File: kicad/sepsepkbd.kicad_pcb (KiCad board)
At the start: 2 copper layers, 162.2 x 115 mm, 62 parts, among them J1 Conn_01x10_Pin, J2 MJ-4PP-9, J3 Conn_01x08_Pin, J4 Conn_01x10_Pin, J5 MJ-4PP-9, J6 Conn_01x08_Pin, J9 Conn_01x10_Pin, SW1 SW_PUSH, SW10 SW_PUSH, SW11 SW_PUSH, SW12 SW_PUSH, SW13 SW_PUSH, SW14 SW_PUSH, SW15 SW_PUSH, SW16 SW_PUSH, SW17 SW_PUSH, SW18 SW_PUSH, SW19 SW_PUSH, SW2 SW_PUSH, SW20 SW_PUSH, SW21 SW_PUSH, SW22 SW_PUSH, SW23 SW_PUSH, SW24 SW_PUSH, SW25 SW_PUSH, SW3 SW_PUSH, SW4 SW_PUSH, SW5 SW_PUSH, SW6 SW_PUSH, SW7 SW_PUSH, SW8 SW_PUSH, SW9 SW_PUSH, U1 RP2040-Zero, U2 RP2040-Zero

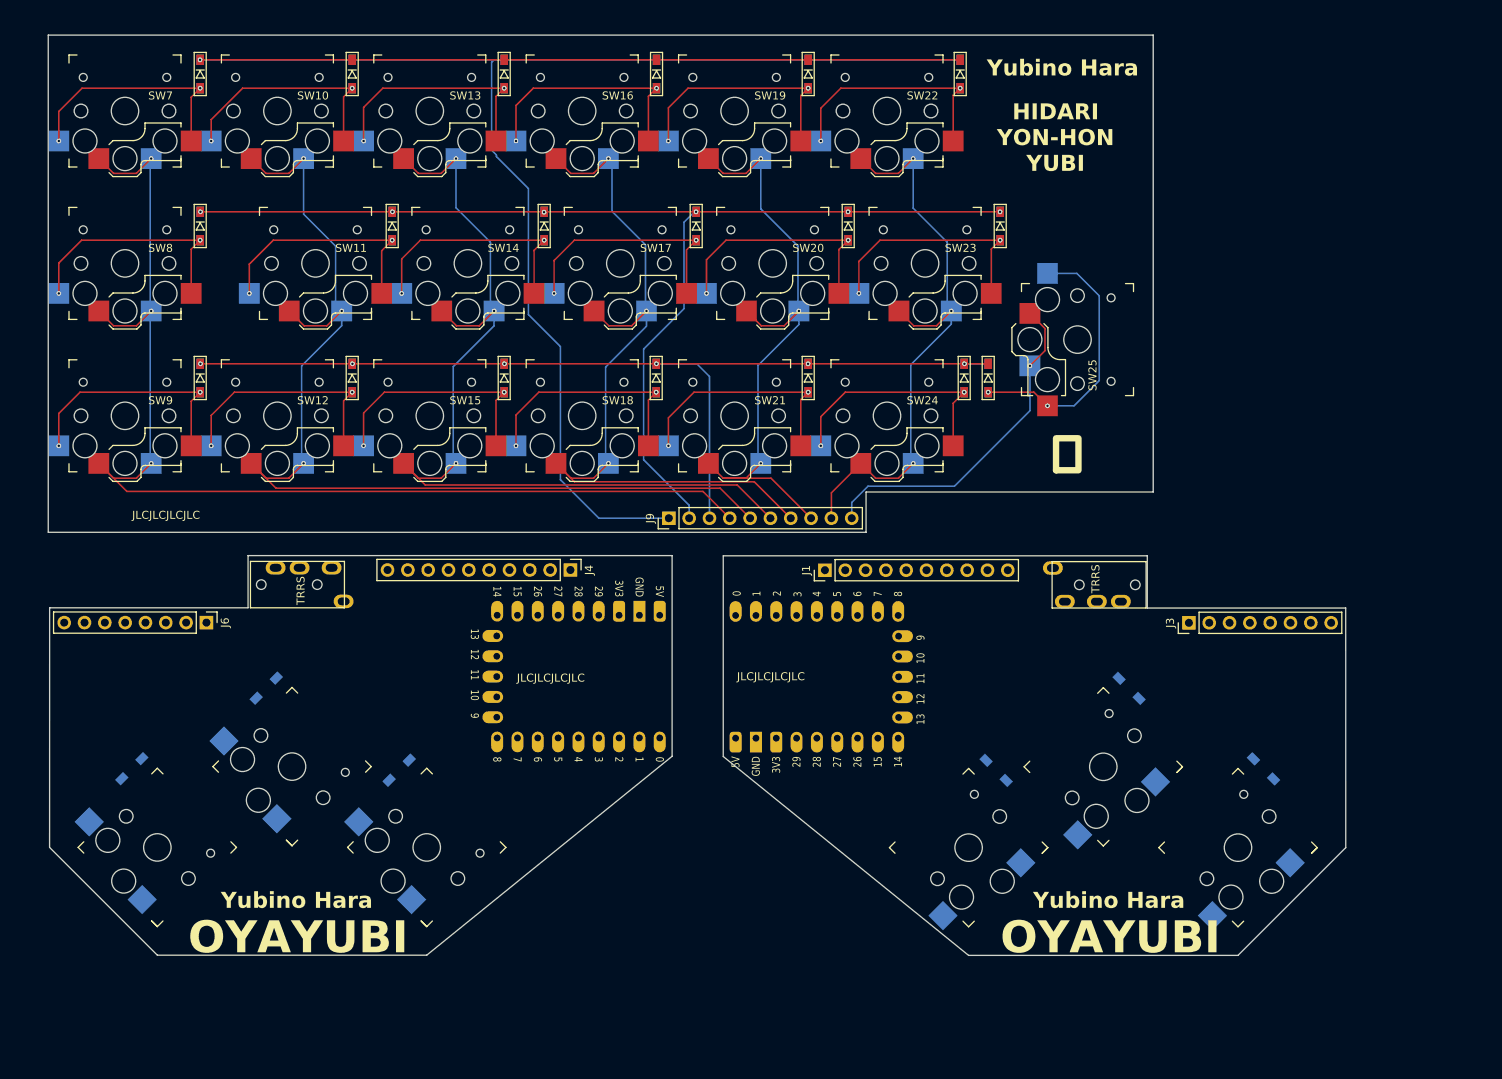
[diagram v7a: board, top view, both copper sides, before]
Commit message: Add LEDs, and convert RP2040 to SMD
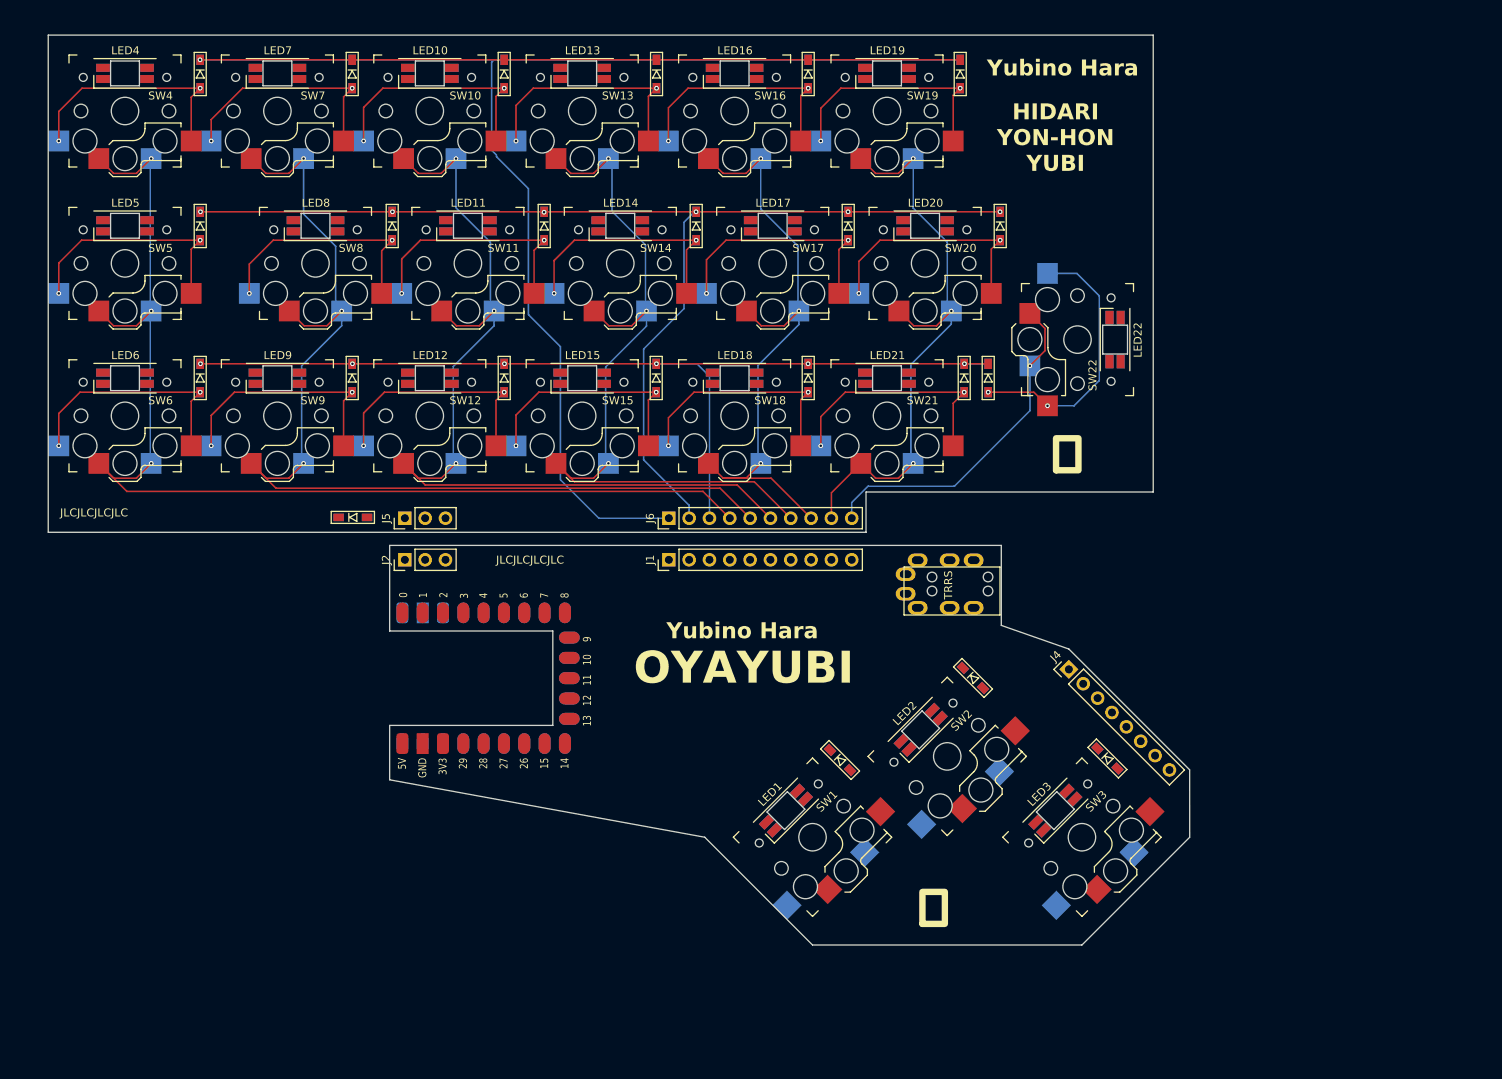
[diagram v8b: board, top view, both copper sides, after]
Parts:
- removed the D4 at (29.9, 109.3)
- removed the D5 at (63.3, 109.5)
- removed the D6 at (46.7, 99.2)
- removed the J4 at (84.7, 84.5)
- removed the J6 at (39.2, 91.0)
- removed the REF** at (48.7, 129.4)
- removed the REF** at (150.2, 129.4)
- removed the SW4 at (33.1, 119.2)
- removed the SW5 at (49.9, 109.0)
- removed the SW6 at (66.7, 119.2)
- removed U2: RP2040-Zero, isw-kbd:RP2040-Zero-THT
- added D23: D, kbd:D3_SMD, F.Cu at (57.5, 77.9)
- added J2: Conn_01x03_Pin, Connector_PinHeader_2.54mm:PinHeader_1x03_P2.54mm_Vertical, F.Cu at (64.0, 83.2)
- added LED1: YS-SK6812MINI-E, sepsepkbd:YS-SK6812MINI-E, F.Cu at (111.6, 114.6)
- added LED10: YS-SK6812MINI-E, sepsepkbd:YS-SK6812MINI-E, F.Cu at (67.1, 22.4)
- added LED11: YS-SK6812MINI-E, sepsepkbd:YS-SK6812MINI-E, F.Cu at (71.9, 41.5)
- added LED12: YS-SK6812MINI-E, sepsepkbd:YS-SK6812MINI-E, F.Cu at (67.1, 60.5)
- added LED13: YS-SK6812MINI-E, sepsepkbd:YS-SK6812MINI-E, F.Cu at (86.2, 22.4)
- added LED14: YS-SK6812MINI-E, sepsepkbd:YS-SK6812MINI-E, F.Cu at (90.9, 41.5)
- added LED15: YS-SK6812MINI-E, sepsepkbd:YS-SK6812MINI-E, F.Cu at (86.2, 60.5)
- added LED16: YS-SK6812MINI-E, sepsepkbd:YS-SK6812MINI-E, F.Cu at (105.2, 22.4)
- added LED17: YS-SK6812MINI-E, sepsepkbd:YS-SK6812MINI-E, F.Cu at (110.0, 41.5)
- added LED18: YS-SK6812MINI-E, sepsepkbd:YS-SK6812MINI-E, F.Cu at (105.2, 60.5)
- added LED19: YS-SK6812MINI-E, sepsepkbd:YS-SK6812MINI-E, F.Cu at (124.3, 22.4)
- added LED2: YS-SK6812MINI-E, sepsepkbd:YS-SK6812MINI-E, F.Cu at (128.5, 104.5)
- added LED20: YS-SK6812MINI-E, sepsepkbd:YS-SK6812MINI-E, F.Cu at (129.0, 41.5)
- added LED21: YS-SK6812MINI-E, sepsepkbd:YS-SK6812MINI-E, F.Cu at (124.3, 60.5)
- added LED22: YS-SK6812MINI-E, sepsepkbd:YS-SK6812MINI-E, F.Cu at (152.8, 55.7)
- added LED3: YS-SK6812MINI-E, sepsepkbd:YS-SK6812MINI-E, F.Cu at (145.3, 114.6)
- added LED4: YS-SK6812MINI-E, sepsepkbd:YS-SK6812MINI-E, F.Cu at (29.0, 22.4)
- added LED5: YS-SK6812MINI-E, sepsepkbd:YS-SK6812MINI-E, F.Cu at (29.0, 41.5)
- added LED6: YS-SK6812MINI-E, sepsepkbd:YS-SK6812MINI-E, F.Cu at (29.0, 60.5)
- added LED7: YS-SK6812MINI-E, sepsepkbd:YS-SK6812MINI-E, F.Cu at (48.1, 22.4)
- added LED8: YS-SK6812MINI-E, sepsepkbd:YS-SK6812MINI-E, F.Cu at (52.8, 41.5)
- added LED9: YS-SK6812MINI-E, sepsepkbd:YS-SK6812MINI-E, F.Cu at (48.1, 60.5)
- added REF**: ThumbsBoard_logo, sepsepkbd:ThumbsBoard_logo, F.Cu at (105.1, 94.3)
- added REF**: ThumbsBoard_logo, sepsepkbd:ThumbsBoard_logo, B.Cu at (105.3, 94.3)
- D1, D2, D3: footprint kbd:D3_SMD_v2 -> kbd:D3_SMD
- J3: renamed from J2; footprint kbd:MJ-4PP-9_1side -> kbd:MJ-4PP-9
- J5: value MJ-4PP-9 -> Conn_01x03_Pin; footprint kbd:MJ-4PP-9_1side -> Connector_PinHeader_2.54mm:PinHeader_1x03_P2.54mm_Vertical
- SW1, SW2, SW3: footprint keyswitches:Kailh_socket_PG1350 -> keyswitches:Kailh_socket_PG1350_reversible
- U1: footprint isw-kbd:RP2040-Zero-THT -> sepsepkbd:WS-RP2040-Zero SMD
- moved U1 41.7 mm to (73.8, 98.0)
- moved J5 21.1 mm to (64.0, 78.0)
- moved D1 19.6 mm to (151.8, 108.0)
- moved D2 19.6 mm to (135.0, 98.0)
- moved D3 19.6 mm to (118.4, 108.2)
- moved J1 19.6 mm to (97.0, 83.2)
- moved SW1 19.6 mm to (115.0, 117.9)
- moved SW2 19.6 mm to (131.8, 107.8)
- moved SW3 19.6 mm to (148.6, 117.9)
- moved J3 18.4 mm to (138.4, 87.1)
- moved J4 16.1 mm to (147.0, 96.9), turned to 45 degrees
- renumbered D13 to D10, D14 to D11, D15 to D12, D16 to D13, D17 to D14, D18 to D15, D19 to D16, D20 to D17, D21 to D18, D22 to D19, D23 to D20, D24 to D21, D25 to D22, D7 to D4, D8 to D5, D9 to D6, D10 to D7, D11 to D8, D12 to D9, J3 to J4, J9 to J6, SW13 to SW10, SW14 to SW11, SW15 to SW12, SW16 to SW13, SW17 to SW14, SW18 to SW15, SW19 to SW16, SW20 to SW17, SW21 to SW18, SW22 to SW19, SW23 to SW20, SW24 to SW21, SW25 to SW22, SW7 to SW4, SW8 to SW5, SW9 to SW6, SW10 to SW7, SW11 to SW8, SW12 to SW9
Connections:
- net bu1_col0 renamed u1_col0
- net bu1_col1 renamed u1_col1
- net bu1_col2 renamed u1_col2
- net bu1_col3 renamed u1_col3
- net bu1_col4 renamed u1_col4
- net bu1_col5 renamed u1_col5
- net bu1_col6 renamed u1_col6
- net bu1_op1 renamed u1_op1
- net bu1_op2 renamed u1_op2
- net bu1_op3 renamed u1_op3
- net bu1_op4 renamed u1_op4
- net bu1_op5 renamed u1_op5
- net bu1_row0 renamed u1_row0
- net bu1_row1 renamed u1_row1
- net bu1_row2 renamed u1_row2
- net bu1_row3 renamed u1_row3
- J3 pad D: u1_3.3v -> u1_5v
- J4 pad 1: bu1_5v -> u1_5v
- U1 pad 14: unconnected-(U1-Pad14) -> u1_led
- U1 pad 32: bu1_5v -> u1_5v
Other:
- board size 162.2 x 115 mm -> 142.7 x 113.7 mm
